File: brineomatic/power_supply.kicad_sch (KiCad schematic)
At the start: 34 parts, among them J10 5.08MM, J9 5.08MM, Q3 20N06, U2 RT7272BGSP, U3 LM74700, U4 MAX40200AUK

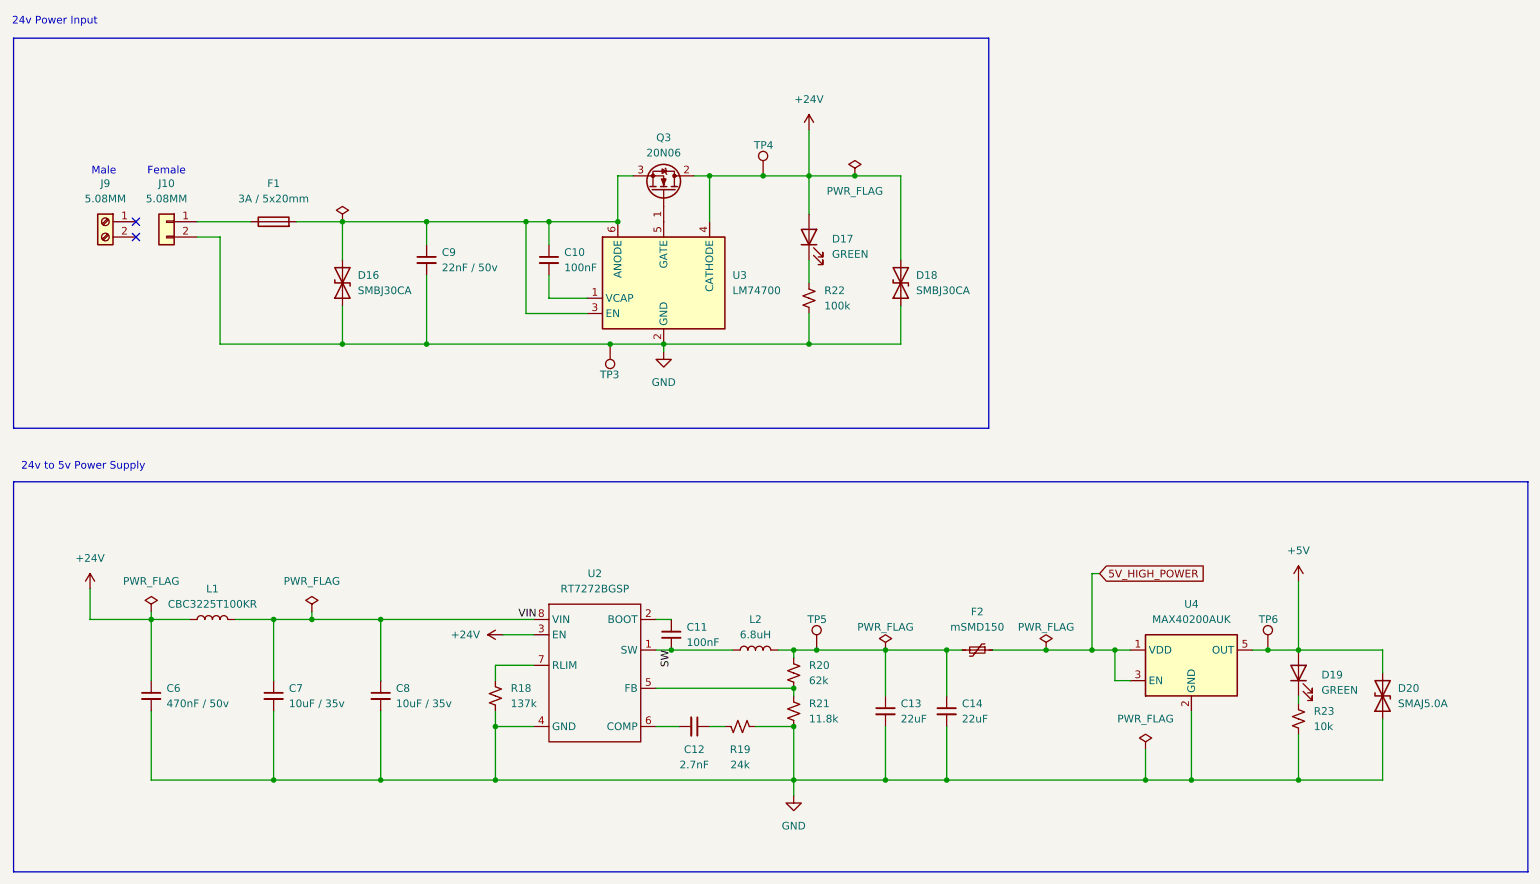
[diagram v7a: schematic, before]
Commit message: added bootstrap diode just in case
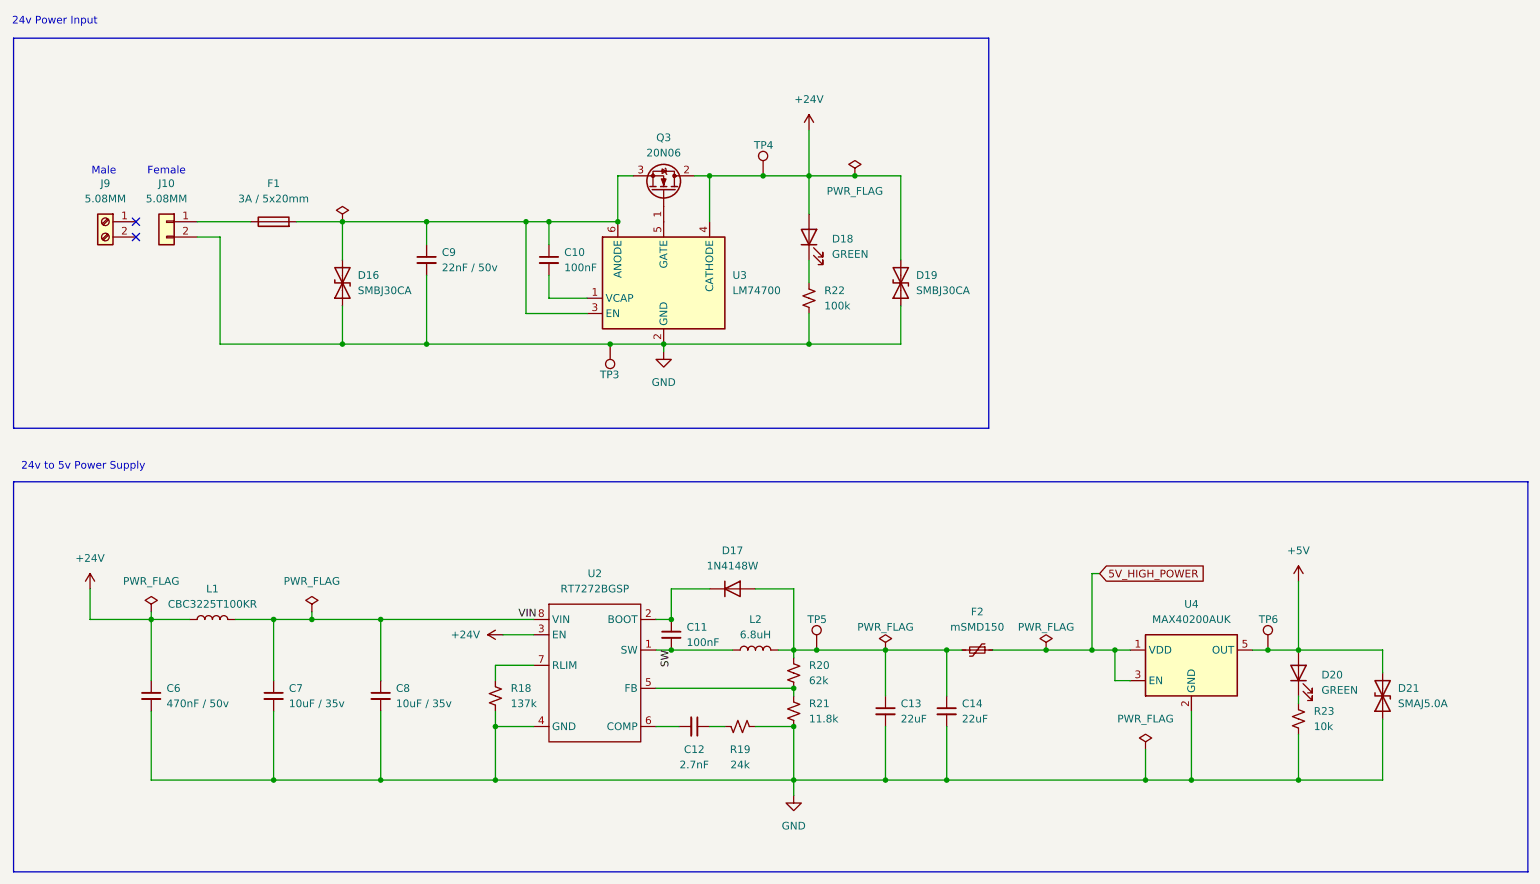
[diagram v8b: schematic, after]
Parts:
- added D17: 1N4148W, Diode_SMD:D_SOD-123, symbol Diode:1N4148W
- renumbered D17 to D18, D18 to D19, D19 to D20, D20 to D21
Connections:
- net at C13.1, C14.1, F2.2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: now also D17.2 (A)
- net at C11.1, U2.2 (BOOT): now also D17.1 (K)
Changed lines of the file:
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@@
 	)
 	(junction
+		(at 130.81 118.11)
+		(diameter 0)
+		(color 0 0 0 0)
+	)
+	(junction
 		(at 166.37 123.19)
 		(diameter 0)
@@
 	(wire
 		(pts
+			(xy 130.81 113.03) (xy 130.81 118.11)
+		)
+		(stroke
+			(width 0)
+			(type default)
+		)
+	)
+	(wire
+		(pts
 			(xy 176.53 123.19) (xy 179.07 123.19)
 		)
@@
 	(wire
 		(pts
+			(xy 151.13 123.19) (xy 151.13 113.03)
+		)
+		(stroke
+			(width 0)
+			(type default)
+		)
+	)
+	(wire
+		(pts
 			(xy 204.47 123.19) (xy 207.01 123.19)
 		)
@@
 	(wire
 		(pts
+			(xy 137.16 113.03) (xy 130.81 113.03)
+		)
+		(stroke
+			(width 0)
+			(type default)
+		)
+	)
+	(wire
+		(pts
 			(xy 153.67 50.8) (xy 153.67 44.45)
 		)
@@
 	(wire
 		(pts
+			(xy 151.13 113.03) (xy 144.78 113.03)
+		)
+		(stroke
+			(width 0)
+			(type default)
+		)
+	)
+	(wire
+		(pts
 			(xy 207.01 128.27) (xy 204.47 128.27)
 		)
@@
 		(dnp no)
 		(fields_autoplaced yes)
-		(property "Reference" "#PWR027"
+		(property "Reference" "#PWR028"
 			(at 129.54 80.01 0)
 			(effects
@@
 			(project "brineomatic"
 				(path "/96477ae2-ef08-48f3-8dd4-fe4478541f68/7cbb3b3c-cf93-4880-b816-c6df902b993c"
-					(reference "#PWR027")
+					(reference "#PWR028")
 					(unit 1)
 				)
@@
 		(dnp no)
 		(fields_autoplaced yes)
-		(property "Reference" "#PWR028"
+		(property "Reference" "#PWR029"
 			(at 151.13 153.67 0)
 			(effects
@@
 			(project "brineomatic"
 				(path "/96477ae2-ef08-48f3-8dd4-fe4478541f68/7cbb3b3c-cf93-4880-b816-c6df902b993c"
-					(reference "#PWR028")
+					(reference "#PWR029")
 					(unit 1)
 				)
@@
 		(dnp no)
 		(fields_autoplaced yes)
-		(property "Reference" "D17"
+		(property "Reference" "D18"
 			(at 157.48 54.9274 90)
 			(effects
@@
 			(project ""
 				(path "/96477ae2-ef08-48f3-8dd4-fe4478541f68/7cbb3b3c-cf93-4880-b816-c6df902b993c"
-					(reference "D17")
+					(reference "D18")
 					(unit 1)
 				)
@@
 		(dnp no)
 		(fields_autoplaced yes)
-		(property "Reference" "#PWR030"
+		(property "Reference" "#PWR031"
 			(at 234.95 115.57 0)
 			(effects
@@
 			(project "brineomatic"
 				(path "/96477ae2-ef08-48f3-8dd4-fe4478541f68/7cbb3b3c-cf93-4880-b816-c6df902b993c"
-					(reference "#PWR030")
+					(reference "#PWR031")
 					(unit 1)
 				)
@@
 		(on_board yes)
 		(dnp no)
-		(property "Reference" "D18"
+		(property "Reference" "D19"
 			(at 171.45 60.96 90)
 			(effects
@@
 			(project "brineomatic"
 				(path "/96477ae2-ef08-48f3-8dd4-fe4478541f68/7cbb3b3c-cf93-4880-b816-c6df902b993c"
-					(reference "D18")
+					(reference "D19")
 					(unit 1)
 				)
@@
 		(dnp no)
 		(fields_autoplaced yes)
-		(property "Reference" "#PWR071"
+		(property "Reference" "#PWR027"
 			(at 106.68 120.65 0)
 			(effects
@@
 			(project "brineomatic"
 				(path "/96477ae2-ef08-48f3-8dd4-fe4478541f68/7cbb3b3c-cf93-4880-b816-c6df902b993c"
-					(reference "#PWR071")
+					(reference "#PWR027")
 					(unit 1)
 				)
@@
 		(dnp no)
 		(fields_autoplaced yes)
-		(property "Reference" "#PWR029"
+		(property "Reference" "#PWR030"
 			(at 153.67 40.64 0)
 			(effects
@@
 			(project "brineomatic"
 				(path "/96477ae2-ef08-48f3-8dd4-fe4478541f68/7cbb3b3c-cf93-4880-b816-c6df902b993c"
-					(reference "#PWR029")
+					(reference "#PWR030")
 					(unit 1)
 				)
@@
 	)
 	(symbol
+		(lib_id "Diode:1N4148W")
+		(at 140.97 113.03 0)
+		(unit 1)
+		(exclude_from_sim no)
+		(in_bom yes)
+		(on_board yes)
+		(dnp no)
+		(fields_autoplaced yes)
+		(property "Reference" "D17"
+			(at 140.97 106.68 0)
+			(effects
+				(font
+					(size 1.27 1.27)
+				)
+			)
+		)
+		(property "Value" "1N4148W"
+			(at 140.97 109.22 0)
+			(effects
+				(font
+					(size 1.27 1.27)
+				)
+			)
+		)
+		(property "Footprint" "Diode_SMD:D_SOD-123"
+			(at 140.97 117.475 0)
+			(effects
+				(font
+					(size 1.27 1.27)
+				)
+				(hide yes)
+			)
+		)
+		(property "Datasheet" "https://www.vishay.com/docs/85748/1n4148w.pdf"
+			(at 140.97 113.03 0)
+			(effects
+				(font
+					(size 1.27 1.27)
+				)
+				(hide yes)
+			)
+		)
+		(property "Description" "75V 0.15A Fast Switching Diode, SOD-123"
+			(at 140.97 113.03 0)
+			(effects
+				(font
+					(size 1.27 1.27)
+				)
+				(hide yes)
+			)
+		)
+		(property "Sim.Device" "D"
+			(at 140.97 113.03 0)
+			(effects
+				(font
+					(size 1.27 1.27)
+				)
+				(hide yes)
+			)
+		)
+		(property "Sim.Pins" "1=K 2=A"
+			(at 140.97 113.03 0)
+			(effects
+				(font
+					(size 1.27 1.27)
+				)
+				(hide yes)
+			)
+		)
+		(pin "2"
+		)
+		(pin "1"
+		)
+		(instances
+			(project ""
+				(path "/96477ae2-ef08-48f3-8dd4-fe4478541f68/7cbb3b3c-cf93-4880-b816-c6df902b993c"
+					(reference "D17")
+					(unit 1)
+				)
+			)
+		)
+	)
+	(symbol
 		(lib_id "Device:R_Small_US")
 		(at 142.24 135.89 90)
@@
 		(dnp no)
 		(fields_autoplaced yes)
-		(property "Reference" "D19"
+		(property "Reference" "D20"
 			(at 238.76 127.3174 90)
 			(effects
@@
 			(project "brineomatic"
 				(path "/96477ae2-ef08-48f3-8dd4-fe4478541f68/7cbb3b3c-cf93-4880-b816-c6df902b993c"
-					(reference "D19")
+					(reference "D20")
 					(unit 1)
 				)
@@
 		(on_board yes)
 		(dnp no)
-		(property "Reference" "D20"
+		(property "Reference" "D21"
 			(at 251.46 129.54 90)
 			(effects
@@
 			(project "brineomatic"
 				(path "/96477ae2-ef08-48f3-8dd4-fe4478541f68/7cbb3b3c-cf93-4880-b816-c6df902b993c"
-					(reference "D20")
+					(reference "D21")
 					(unit 1)
 				)
